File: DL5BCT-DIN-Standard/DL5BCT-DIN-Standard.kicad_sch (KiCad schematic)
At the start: 1 part, among them J1 DIN-5_180degree

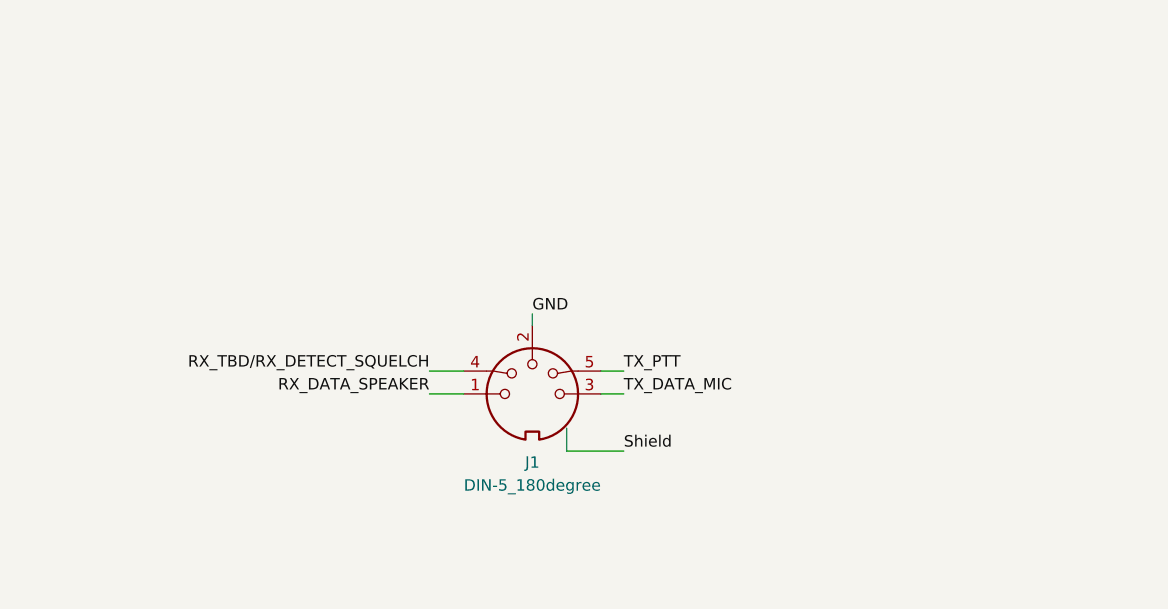
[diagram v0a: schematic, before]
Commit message: Added 'text table' with cable colour conventions. 	modified:   DL5BCT-DIN-Adapter-Mic-4pol-Sommerkamp_FT-277E/DL5BCT-DIN-Adapter-Mic-4pol-Sommerkamp_FT-277E.kicad_sch 	modified:   DL5BCT-DIN-Adapter-Mic-6pol-Kenwood_Trio_TR9000/DL5BCT-DIN-Adapter-Mic-6pol-Kenwood_Trio_TR9000.kicad_sch 	modified:   DL5BCT-DIN-Standard/DL5BCT-DIN-Standard.kicad_sch
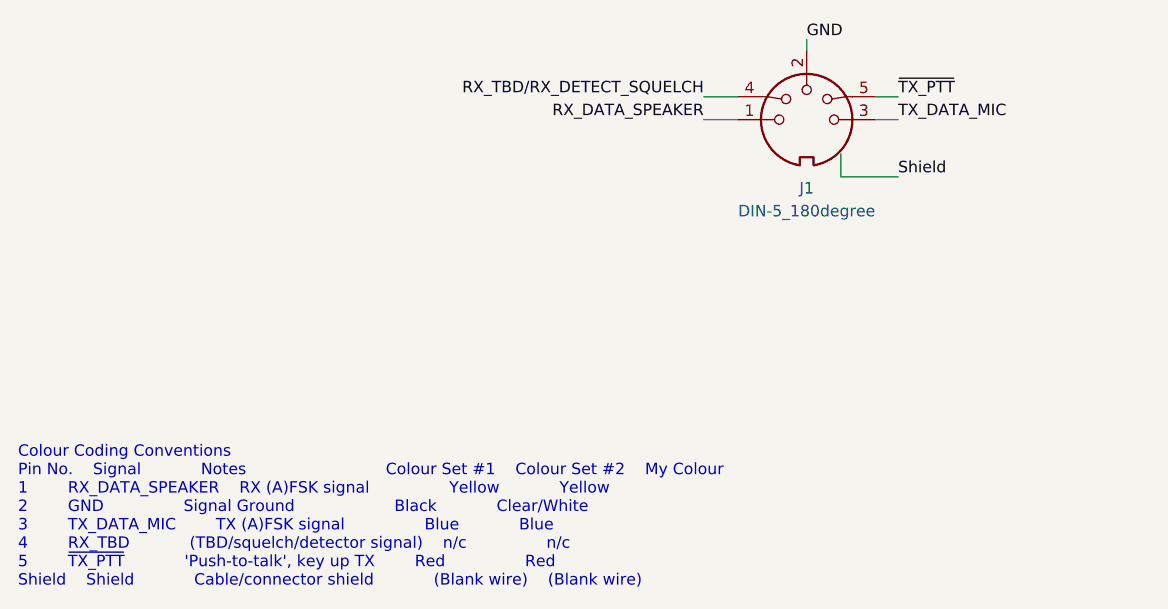
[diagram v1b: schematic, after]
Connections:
- net TX_PTT renamed ~{TX_PTT}
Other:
- note added: "Colour Coding Conventions Pin No. Signal Notes Colour Set #1 Colour Set #2 My Colour 1 RX_DATA_SPEAKER RX (A)FSK signal Yellow Yellow 2 GND Signal Ground Black Clear/White 3 TX_DATA_MIC TX (A)FSK signal Blue Blue 4 RX_TBD (TBD/squelch/detector signal) n/c n/c 5 ~{TX_PTT} 'Push-to-talk', key up TX Red Red Shield Shield Cable/connector shield (Blank wire) (Blank wire)"
- moved on the sheet: J1
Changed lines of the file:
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@@
 (kicad_sch (version 20211123) (generator eeschema)
-  (paper "A5" portrait)
+  (paper "A5")
   (title_block
     (title "DL5BCT DIN Standard Pinout")
@@
     (comment 3 "Standard DIN connector pinout by DL5BCT")
   )
-  (wire (pts (xy 74.93 67.31) (xy 74.93 68.58))
+  (wire (pts (xy 105.41 36.83) (xy 105.41 38.1))
     (stroke (width 0) (type default) (color 0 0 0 0))
   )
-  (wire (pts (xy 82.55 76.2) (xy 85.09 76.2))
+  (wire (pts (xy 113.03 45.72) (xy 115.57 45.72))
     (stroke (width 0) (type default) (color 0 0 0 0))
   )
-  (wire (pts (xy 78.74 82.55) (xy 85.09 82.55))
+  (wire (pts (xy 109.22 52.07) (xy 115.57 52.07))
     (stroke (width 0) (type default) (color 0 0 0 0))
   )
-  (wire (pts (xy 63.5 76.2) (xy 67.31 76.2))
+  (wire (pts (xy 93.98 45.72) (xy 97.79 45.72))
     (stroke (width 0) (type default) (color 0 0 0 0))
   )
-  (wire (pts (xy 63.5 73.66) (xy 67.31 73.66))
+  (wire (pts (xy 93.98 43.18) (xy 97.79 43.18))
     (stroke (width 0) (type default) (color 0 0 0 0))
   )
-  (wire (pts (xy 82.55 73.66) (xy 85.09 73.66))
+  (wire (pts (xy 113.03 43.18) (xy 115.57 43.18))
     (stroke (width 0) (type default) (color 0 0 0 0))
   )
-  (wire (pts (xy 78.74 80.01) (xy 78.74 82.55))
+  (wire (pts (xy 109.22 49.53) (xy 109.22 52.07))
     (stroke (width 0) (type default) (color 0 0 0 0))
   )
-  (label "RX_DATA_SPEAKER" (at 63.5 76.2 180)
+  (text "Colour Coding Conventions\nPin No.	Signal			Notes							Colour Set #1	Colour Set #2	My Colour\n1		RX_DATA_SPEAKER	RX (A)FSK signal				Yellow			Yellow\n2		GND				Signal Ground					Black			Clear/White\n3		TX_DATA_MIC		TX (A)FSK signal				Blue			Blue\n4		RX_TBD			(TBD/squelch/detector signal)	n/c				n/c\n5		~{TX_PTT}			'Push-to-talk', key up TX		Red				Red\nShield	Shield			Cable/connector shield			(Blank wire)	(Blank wire)"
+    (at 17.78 97.79 0)
+    (effects (font (size 1.27 1.27)) (justify left bottom))
+  )
+  (label "RX_DATA_SPEAKER" (at 93.98 45.72 180)
     (effects (font (size 1.27 1.27)) (justify right bottom))
   )
-  (label "RX_TBD{slash}RX_DETECT_SQUELCH" (at 63.5 73.66 180)
+  (label "RX_TBD{slash}RX_DETECT_SQUELCH" (at 93.98 43.18 180)
     (effects (font (size 1.27 1.27)) (justify right bottom))
   )
-  (label "TX_DATA_MIC" (at 85.09 76.2 0)
+  (label "TX_DATA_MIC" (at 115.57 45.72 0)
     (effects (font (size 1.27 1.27)) (justify left bottom))
   )
-  (label "GND" (at 74.93 67.31 0)
+  (label "GND" (at 105.41 36.83 0)
     (effects (font (size 1.27 1.27)) (justify left bottom))
   )
-  (label "TX_PTT" (at 85.09 73.66 0)
+  (label "~{TX_PTT}" (at 115.57 43.18 0)
     (effects (font (size 1.27 1.27)) (justify left bottom))
   )
-  (label "Shield" (at 85.09 82.55 0)
+  (label "Shield" (at 115.57 52.07 0)
     (effects (font (size 1.27 1.27)) (justify left bottom))
   )
-  (symbol (lib_id "Connector:DIN-5_180degree") (at 74.93 76.2 0) (unit 1)
+  (symbol (lib_id "Connector:DIN-5_180degree") (at 105.41 45.72 0) (unit 1)
     (in_bom yes) (on_board yes) (fields_autoplaced)
-    (property "Reference" "J1" (id 0) (at 74.9301 83.82 0))
-    (property "Value" "DIN-5_180degree" (id 1) (at 74.9301 86.36 0))
-    (property "Footprint" "" (id 2) (at 74.93 76.2 0)
+    (property "Reference" "J1" (id 0) (at 105.4101 53.34 0))
+    (property "Value" "DIN-5_180degree" (id 1) (at 105.4101 55.88 0))
+    (property "Footprint" "" (id 2) (at 105.41 45.72 0)
       (effects (font (size 1.27 1.27)) hide)
     )
-    (property "Datasheet" "http://www.mouser.com/ds/2/18/40_c091_abd_e-75918.pdf" (id 3) (at 74.93 76.2 0)
+    (property "Datasheet" "http://www.mouser.com/ds/2/18/40_c091_abd_e-75918.pdf" (id 3) (at 105.41 45.72 0)
       (effects (font (size 1.27 1.27)) hide)
     )

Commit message: Settled name of squelch signal, amended sheet comments with connector direction 	modified:   DL5BCT-DIN-Standard/DL5BCT-DIN-Standard.kicad_sch
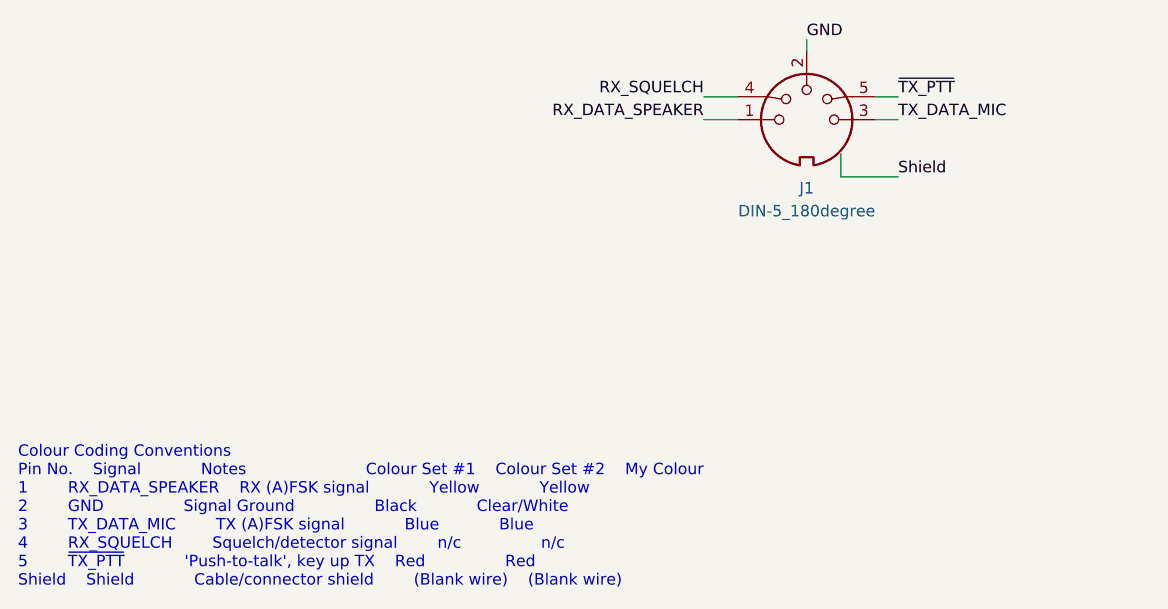
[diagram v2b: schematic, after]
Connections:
- net RX_TBD/RX_DETECT_SQUELCH renamed RX_SQUELCH
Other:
- note added: "Colour Coding Conventions Pin No. Signal Notes Colour Set #1 Colour Set #2 My Colour 1 RX_DATA_SPEAKER RX (A)FSK signal Yellow Yellow 2 GND Signal Ground Black Clear/White 3 TX_DATA_MIC TX (A)FSK signal Blue Blue 4 RX_SQUELCH Squelch/detector signal n/c n/c 5 ~{TX_PTT} 'Push-to-talk', key up TX Red Red Shield Shield Cable/connector shield (Blank wire) (Blank wire)"
- note removed: "Colour Coding Conventions Pin No. Signal Notes Colour Set #1 Colour Set #2 My Colour 1 RX_DATA_SPEAKER RX (A)FSK signal Yellow Yellow 2 GND Signal Ground Black Clear/White 3 TX_DATA_MIC TX (A)FSK signal Blue Blue 4 RX_TBD (TBD/squelch/detector signal) n/c n/c 5 ~{TX_PTT} 'Push-to-talk', key up TX Red Red Shield Shield Cable/connector shield (Blank wire) (Blank wire)"
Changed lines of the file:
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@@
   (title_block
     (title "DL5BCT DIN Standard Pinout")
-    (date "2023-01-07")
-    (rev "V1.0")
+    (date "2023-02-11")
+    (rev "V1.0.1")
     (company "Peter Cornelius DL5BCT / peter cornelius consulting")
-    (comment 1 "Radio acts as 'amplifier', computer acts as 'recorder'.")
-    (comment 2 "Derived from the DIN 41524 standard audio pinout:")
-    (comment 3 "Standard DIN connector pinout by DL5BCT")
+    (comment 1 "The connector at the radio side (mike 'plug') per default is female.")
+    (comment 2 "Radio acts as 'amplifier', computer acts as 'recorder'.")
+    (comment 3 "Derived from the DIN 41524 standard audio pinout:")
+    (comment 4 "Standard DIN connector pinout by DL5BCT")
   )
   (wire (pts (xy 105.41 36.83) (xy 105.41 38.1))
@@
     (stroke (width 0) (type default) (color 0 0 0 0))
   )
-  (text "Colour Coding Conventions\nPin No.	Signal			Notes							Colour Set #1	Colour Set #2	My Colour\n1		RX_DATA_SPEAKER	RX (A)FSK signal				Yellow			Yellow\n2		GND				Signal Ground					Black			Clear/White\n3		TX_DATA_MIC		TX (A)FSK signal				Blue			Blue\n4		RX_TBD			(TBD/squelch/detector signal)	n/c				n/c\n5		~{TX_PTT}			'Push-to-talk', key up TX		Red				Red\nShield	Shield			Cable/connector shield			(Blank wire)	(Blank wire)"
+  (text "Colour Coding Conventions\nPin No.	Signal			Notes						Colour Set #1	Colour Set #2	My Colour\n1		RX_DATA_SPEAKER	RX (A)FSK signal			Yellow			Yellow\n2		GND				Signal Ground				Black			Clear/White\n3		TX_DATA_MIC		TX (A)FSK signal			Blue			Blue\n4		RX_SQUELCH		Squelch/detector signal		n/c				n/c\n5		~{TX_PTT}			'Push-to-talk', key up TX	Red				Red\nShield	Shield			Cable/connector shield		(Blank wire)	(Blank wire)"
     (at 17.78 97.79 0)
     (effects (font (size 1.27 1.27)) (justify left bottom))
@@
     (effects (font (size 1.27 1.27)) (justify right bottom))
   )
-  (label "RX_TBD{slash}RX_DETECT_SQUELCH" (at 93.98 43.18 180)
+  (label "RX_SQUELCH" (at 93.98 43.18 180)
     (effects (font (size 1.27 1.27)) (justify right bottom))
   )
